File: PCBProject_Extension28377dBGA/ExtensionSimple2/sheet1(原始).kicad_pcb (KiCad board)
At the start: 4 copper layers, 122.2 x 82.1 mm, 114 parts, among them J1 Conn_02x05_Odd_Even, J2 Conn_01x02_Pin, J3 Conn_01x02_Pin, J4 CAN_1_CONNECT, J5 RS485_1_CONNECT, J6 CAN_2_CONNECT, J7 RS485_2_CONNECT, Q1 FMMT618TA, U1 SN74ABT541, U2 SN74ABT541, U4 SN65HVD230, U5 SN65HVD230

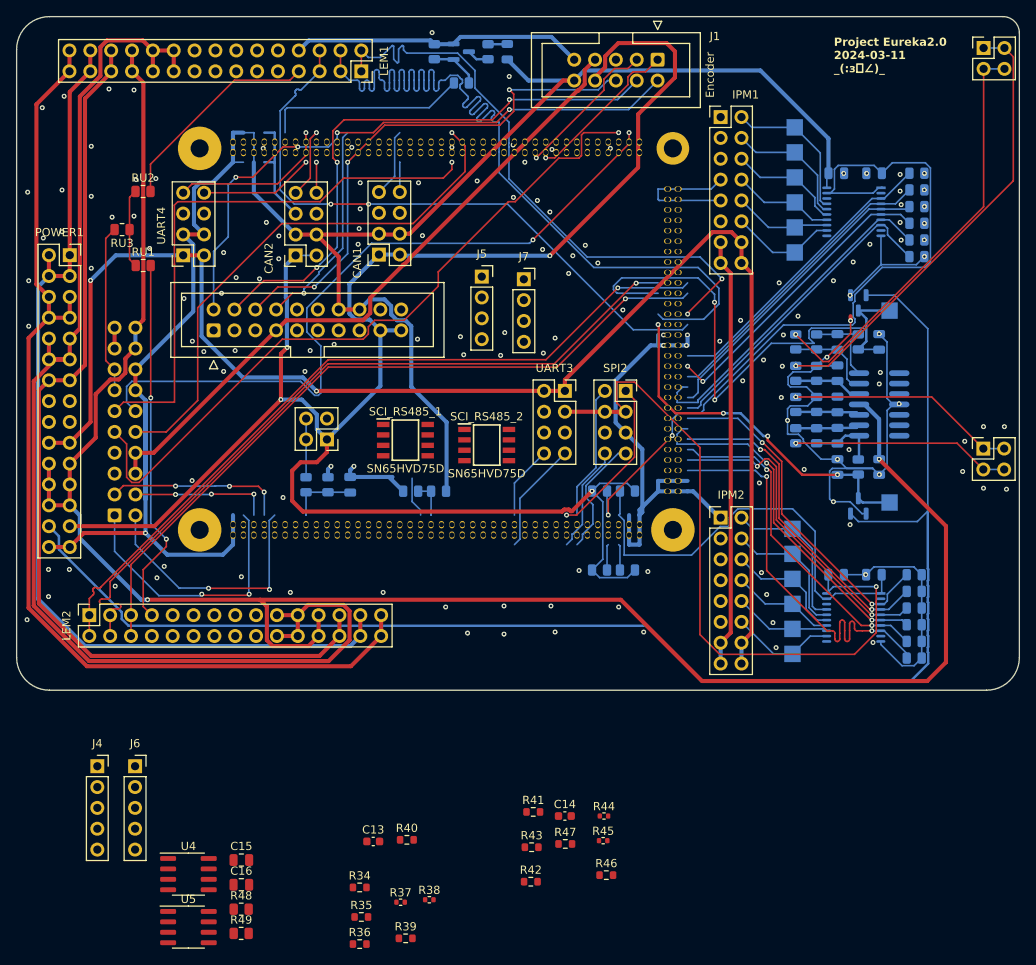
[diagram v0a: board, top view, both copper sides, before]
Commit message: 确定底板尺寸，目前只差布线
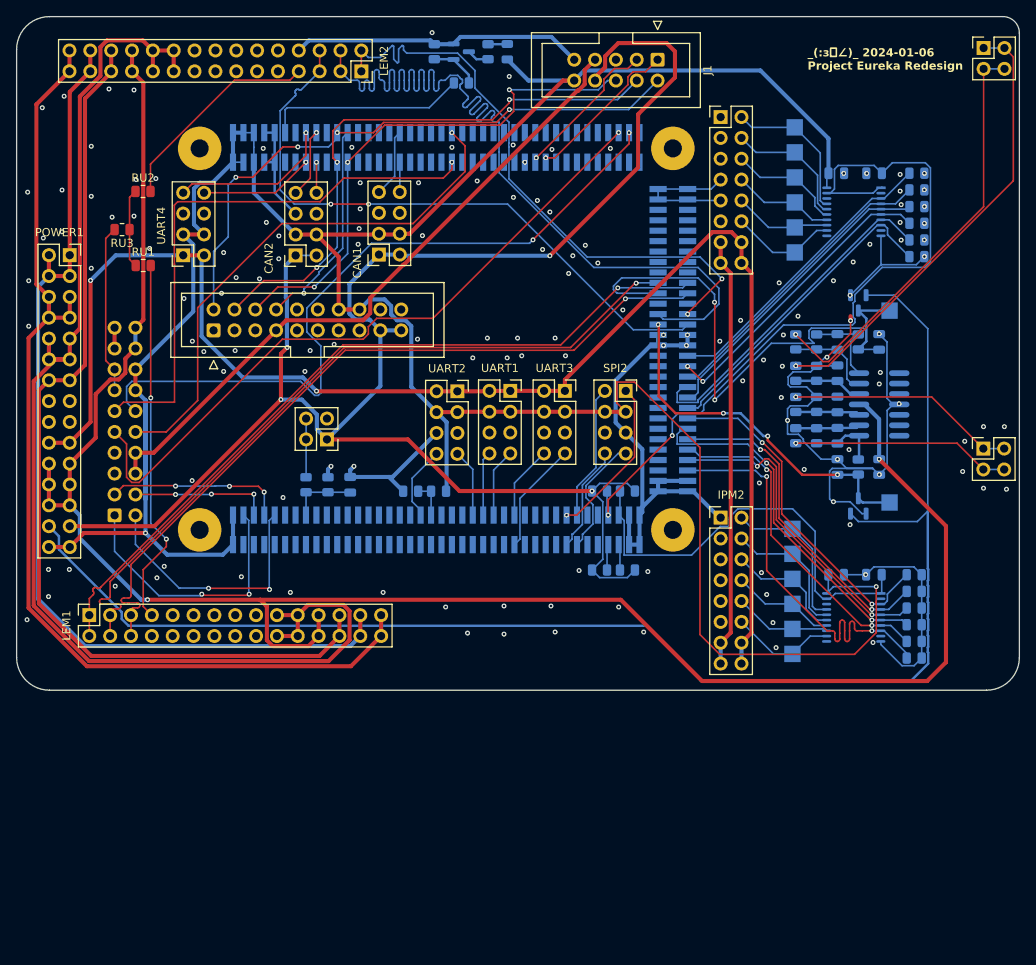
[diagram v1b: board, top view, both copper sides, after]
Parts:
- removed C13, C14: 0.1uF, Capacitor_SMD:C_0603_1608Metric
- removed C15, C16: 104, Capacitor_SMD:C_0805_2012Metric
- removed J4: CAN_1_CONNECT, Connector_PinSocket_2.54mm:PinSocket_1x05_P2.54mm_Vertical
- removed J5: RS485_1_CONNECT, Connector_PinSocket_2.54mm:PinSocket_1x04_P2.54mm_Vertical
- removed J6: CAN_2_CONNECT, Connector_PinSocket_2.54mm:PinSocket_1x05_P2.54mm_Vertical
- removed J7: RS485_2_CONNECT, Connector_PinSocket_2.54mm:PinSocket_1x04_P2.54mm_Vertical
- removed R34, R35, R39, R40, R41, R42, R46, R47: 10K, Resistor_SMD:R_0603_1608Metric
- removed R36, R43: 120R, Resistor_SMD:R_0603_1608Metric
- removed R37, R38, R44, R45: 10R, Resistor_SMD:R_0402_1005Metric
- removed R48, R49: 4.7k, Resistor_SMD:R_0805_2012Metric
- removed SCI_RS485_1, SCI_RS485_2: SN65HVD75D, Oshinoko:SOIC127P600X175-8N
- removed U4, U5: SN65HVD230, Package_SO:SOIC-8_3.9x4.9mm_P1.27mm
- added UART1: Conn_02x04_Counter_Clockwise, Connector_PinSocket_2.54mm:PinSocket_2x04_P2.54mm_Vertical, F.Cu at (252.0, 119.6)
- added UART2: Conn_02x04_Counter_Clockwise, Connector_PinSocket_2.54mm:PinSocket_2x04_P2.54mm_Vertical, F.Cu at (245.5, 119.6)
- DSP1: footprint Oshinoko:DSP_240_0p6mm -> 1mmlab_footprint:DSP_240_SMD
- N1: footprint Oshinoko:SOIC14_M -> 1mmlab_footprint:SOIC14_M
- R21, R22: value 1K -> 1k
- R31: value 1K -> 301R
- U1, U2: footprint Oshinoko:TSSOP-20 -> 1mmlab_footprint:TSSOP-20
- renumbered LEM2 to LEM1, LEM1 to LEM2
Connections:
- C1 pad 1: unconnected-(C1-Pad1) -> AGND
- C1 pad 2: unconnected-(C1-Pad2) -> /DSP_PWM1~{_ENABL}E
- DSP1 pad 133: /UART_WRB -> unconnected-(DSP1-133_GP134-Pad133)
- DSP1 pad 141: /UART_WRA -> unconnected-(DSP1-141_GP132-Pad141)
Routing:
- net D+5V: track 338.5 -> 354.1 mm
- net VDD: track 230.3 -> 216.5 mm
- net /UART_SCI_TXDA: track 0.00 -> 8.35 mm
- net /UART_SCI_RXDB: track 0.00 -> 8.24 mm
- net /UART_SCI_RXDA: track 0.00 -> 7.83 mm
- net AGND: track 252.1 -> 259.8 mm, vias 143 -> 145
- net /UART_SCI_TXDB: track 4.92 -> 9.13 mm
- net /IPM_IU2: track 90.2 -> 93.9 mm
- net /SPI_A_MO_HS: track 87.0 -> 84.5 mm
- net D12V1: track 178.8 -> 179.4 mm
- net unconnected-(C1-Pad1): track 0.14 -> 0.00 mm, vias 1 -> 0
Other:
- board text added: "_(:з」∠)_ 2024-01-06 Project Eureka Redesign"
- board text removed: "Encoder"
- board text removed: "IPM1"
- board text removed: "Project Eureka2.0 2024-03-11 _(:з」∠)_"
